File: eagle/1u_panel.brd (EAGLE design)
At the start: 82 x 100 mm, 54 parts, among them J1 1.27MM-SWD-CONNECTOR, U1 SPV1040, U5 P-CHANNELFET, U6 ON-N-CHANNEL-FET, U7 DIODE-INC-NPNSOT23HOLE

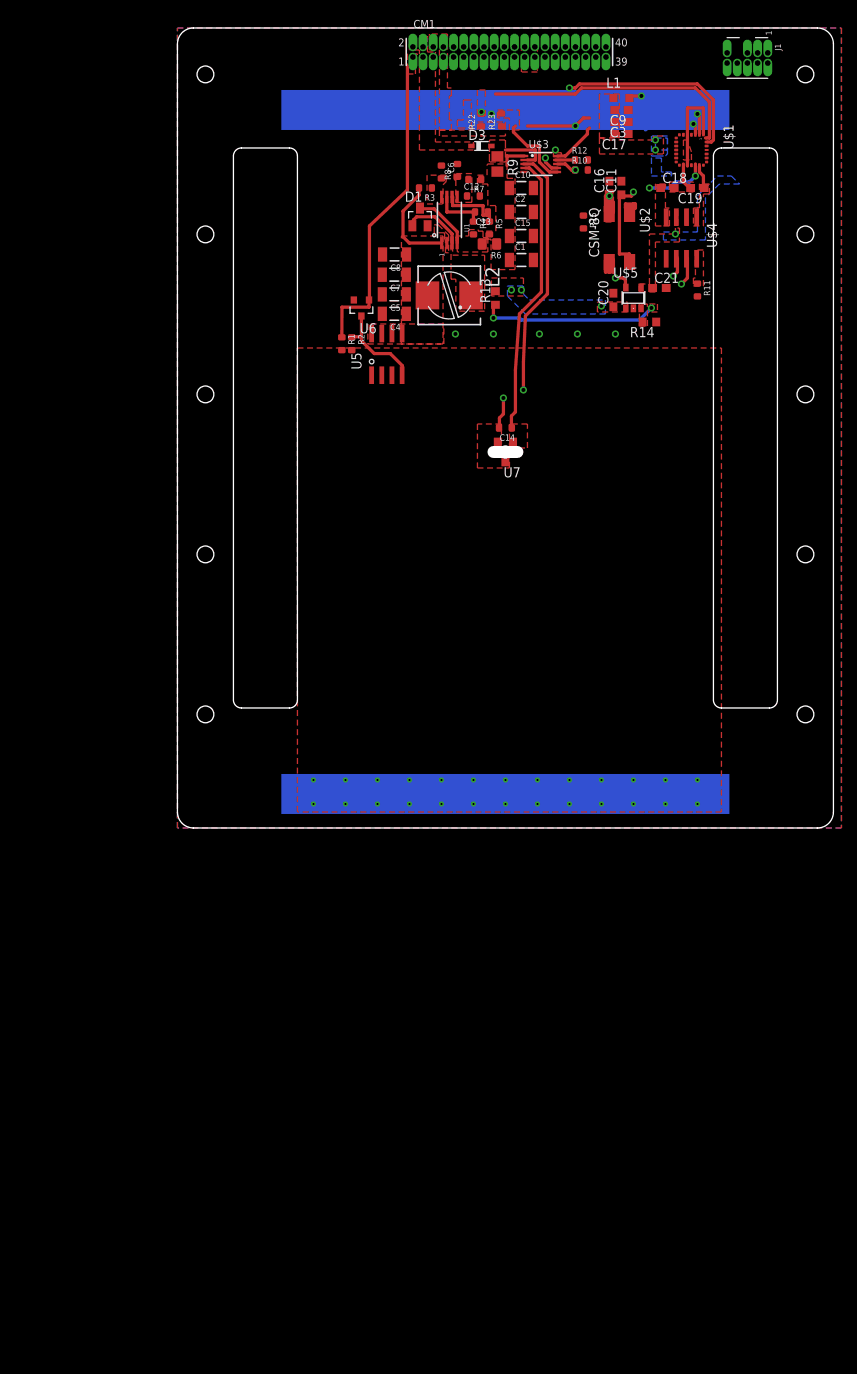
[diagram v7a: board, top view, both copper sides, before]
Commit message: Lots o' changes: Moved to the TCAN330 can controller. Looked for a new SPS chip, but Austin found a really good one, couldn't justify switching to a lower power one in a smaller package because 0.5 mm, ick. Also redid the QFN layout of the STM, fixed a bunch of ERC errors. Left to do: some R and C values, think closely about the LQFP package, and switch to the new 12 pin connector.
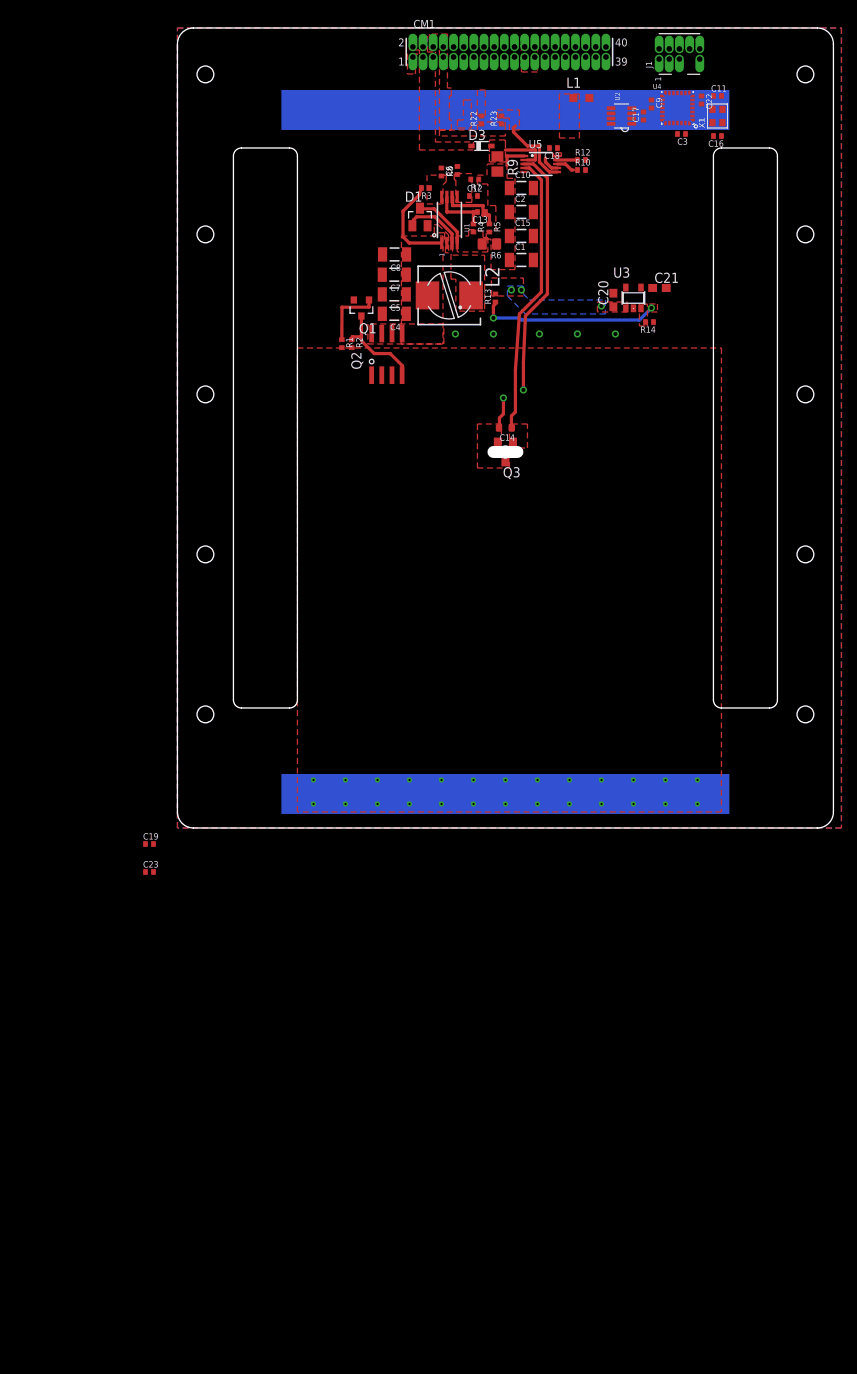
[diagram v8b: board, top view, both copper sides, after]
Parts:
- removed R11: 0, rcl_custom:.0603-B-NOSILK
- removed R15: (no value), rcl_custom:.0603-B-NOSILK
- removed U$1: STM32F042, STM32F042F6:UFQFPN-28
- removed U$2: CSM-8Q, CSM-8Q:4-SMD
- removed U$3: LTC2990, LTC2990:MSOP10
- removed U$4: SN65HVD231, SN65HVD231:SO-08
- added C22, C23: 100n, rcl_custom:.0402-B-NOSILK
- added Q2: P-CHANNELFET, vishay-p-channel-fet:SO8
- added U2: TCAN330, TCAN330:SOT23-8_TI-DCN
- added U4: STM32F042G, STM32F042G:UFQFPN-28
- added X1: 8MHZ-2.5x2mm, low-gain-radio:CRYSTAL_2.5X2
- C11, C16: value (none) -> 20p?; device rcl:C0603 -> rcl_custom:.0402-B-NOSILK
- C12, C13, C6: value .1u -> 100n; device rcl_custom:.0603-B-NOSILK -> rcl_custom:.0402-B-NOSILK
- C17, C18, C19, C3, C9: value (none) -> 100n; device rcl:C0603 -> rcl_custom:.0402-B-NOSILK
- R1, R10, R12, R2, R22, R23, R3, R4, R5, R7, R8: device rcl_custom:.0603-B-NOSILK -> rcl_custom:.0402-B-NOSILK
- R13: value 10k -> 100k; device rcl:R0603 -> rcl_custom:.0402-B-NOSILK
- R14: value 10k -> 33.3k; device rcl:R0603 -> rcl_custom:.0402-B-NOSILK
- U3: value LM3761 -> LM3671MF-3.3
- U5: value P-CHANNELFET -> LTC2990; device vishay-p-channel-fet:SO8 -> LTC2990:MSOP10
- moved C19 106.8 mm to (-3.50, -2.00), turned to 0 degrees
- moved U5 30.6 mm to (45.4, 83.0), turned to 270 degrees
- moved C11 16.6 mm to (67.5, 91.5), turned to 0 degrees
- moved C18 15.1 mm to (47.0, 85.0), turned to 180 degrees
- moved C16 15.0 mm to (67.5, 86.5), turned to 180 degrees
- moved J1 8.51 mm to (62.8, 96.8), turned to 90 degrees
- moved C3 7.65 mm to (63.0, 86.8)
- moved L1 5.00 mm to (50.5, 91.2)
- moved C9 3.82 mm to (59.2, 90.5), turned to 270 degrees
- moved C17 3.55 mm to (58.2, 89.0), turned to 90 degrees
- renumbered U$5 to U3, U6 to Q1, U7 to Q3
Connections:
- removed net D: C19.1, U$1.20, U$4.1
- removed net R: C18.1, U$1.19, U$4.4
- removed net R11: R11.1, U$4.8
- removed net SCLOPT1: R22.2, U$1.28, U$3.7
- removed net SCLOPT2: R23.2, U$1.27, U$3.6
- removed net SWDCLK: J1.SWDCLK, U$1.22
- removed net SWO: J1.SWO, U$1.23
- removed net TDI: J1.NC, U$1.14
- new net CAN_EN: U2.5, U4.13
- new net CAN_LSTN: U2.8, U4.12
- new net CAN_RX: U2.4, U4.19
- new net CAN_TX: U2.1, U4.20
- new net SCL: R22.2, U4.27, U5.7
- new net SDA: R23.2, U4.28, U5.6
- new net SWCLK: J1.SWDCLK, U4.22
- net 3.3V: now also C19.1, C22.2, U2.3, U4.17, U4.18, U4.5; no longer R15.2, R22.1, R23.1, U$1.1, U$1.17, U$1.5, U$3.10, U$4.3
- net ADDRSELECT: now also U5.8; no longer U$3.8
- net ADR1: now also U5.9; no longer U$3.9
- net CANH: now also U2.7; no longer U$4.7
- net CANL: now also U2.6; no longer U$4.6
- net CRYSTALIN: now also U4.2, X1.1; no longer U$1.2, U$2.1
- net CRYSTALOUT: now also U4.3, X1.3; no longer U$1.3, U$2.3
- net GND: now also C22.1, C23.2, U2.2, U4.16, U5.5, X1.2, X1.4; no longer R11.2, U$1.16, U$2.2, U$2.4, U$3.5, U$4.2
- net N6: now also Q2.4; no longer U5.4
- net RESET: now also U4.4; no longer R15.1, U$1.4
- net SOLAR-IN: now also Q2.1, Q2.2, Q2.3; no longer U5.1, U5.2, U5.3
- net SOLAR-IN-SWITCHED: now also C20.1, C23.1, Q2.5, Q2.6, Q2.7, Q2.8, R13.2, U3.1; no longer U5.5, U5.6, U5.7, U5.8
- net SOLAR-IN-SWITCHED2: now also C18.1, R22.1, R23.1, U5.1, U5.10; no longer C20.1, R13.2, U$3.1, U3.1
- net SWDIO: now also U4.21; no longer U$1.21
- net V3: now also U5.3; no longer U$3.3
- net V4: now also U5.4; no longer U$3.4
- net VSOLAR: now also U5.2; no longer U$3.2
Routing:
- net CANH: track 60.3 -> 0.00 mm, vias 1 -> 0
- net CANL: track 55.5 -> 0.00 mm, vias 1 -> 0
- net SCLOPT2: track 38.1 -> 0.00 mm, vias 2 -> 0
- net CRYSTALOUT: track 34.6 -> 0.00 mm, vias 2 -> 0
- net CRYSTALIN: track 34.4 -> 0.00 mm, vias 2 -> 0
- net SDAOPT2: track 32.8 -> 0.00 mm
- net STEPD: track 31.1 -> 0.00 mm, vias 2 -> 0
- net SHORT: track 39.3 -> 8.35 mm
- net ADDRSELECT: track 23.5 -> 2.31 mm, vias 1 -> 0
- net VCCOPT1: track 16.6 -> 0.00 mm, vias 2 -> 0
- net SCLOPT1: track 15.5 -> 0.00 mm, vias 2 -> 0
- net GND: track 15.3 -> 0.00 mm
- net 3.3V: track 12.5 -> 0.00 mm, vias 3 -> 0
- net R: track 7.87 -> 0.00 mm, vias 2 -> 0
- net D: track 2.96 -> 0.00 mm
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- added copper zone on layer 1, net SCL
- removed copper zone on layer 16, net 3.3V
- removed copper zone on layer 1, net CRYSTALIN
- removed copper zone on layer 1, net D
- removed copper zone on layer 1, net R
- removed copper zone on layer 1, net R11
- removed copper zone on layer 1, net SCLOPT1
